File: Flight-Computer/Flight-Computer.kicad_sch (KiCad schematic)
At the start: 40 parts, among them J1 Jumper_NO, J2 Jumper_NO, P1 647676-2, P2 1546551-2, P3 3220-20-0200-00, U1 STM32H750VBTx, U2 LMS8117AMP-3.3_NOPB, Y1 ECS-240-18-33-JGN-TR

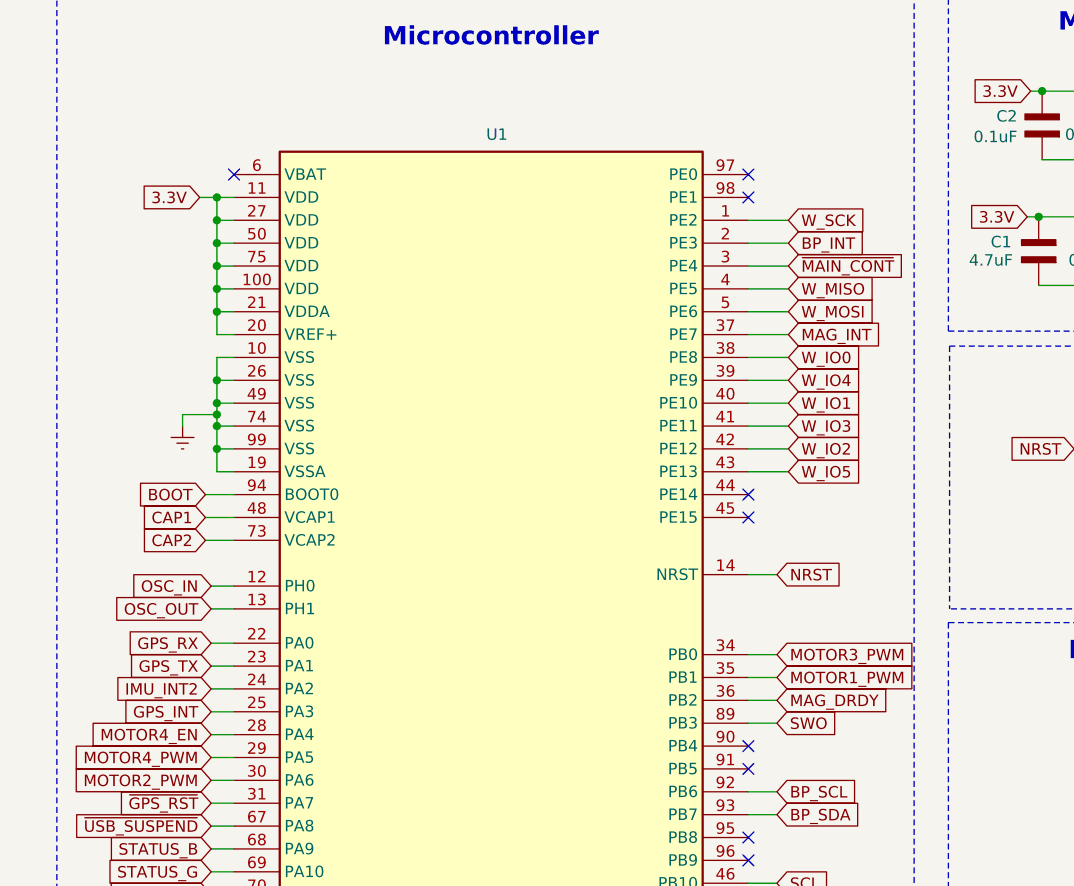
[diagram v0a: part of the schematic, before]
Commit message: SPI Flash Daisy chain
need to review and likely rewire the daisy chain
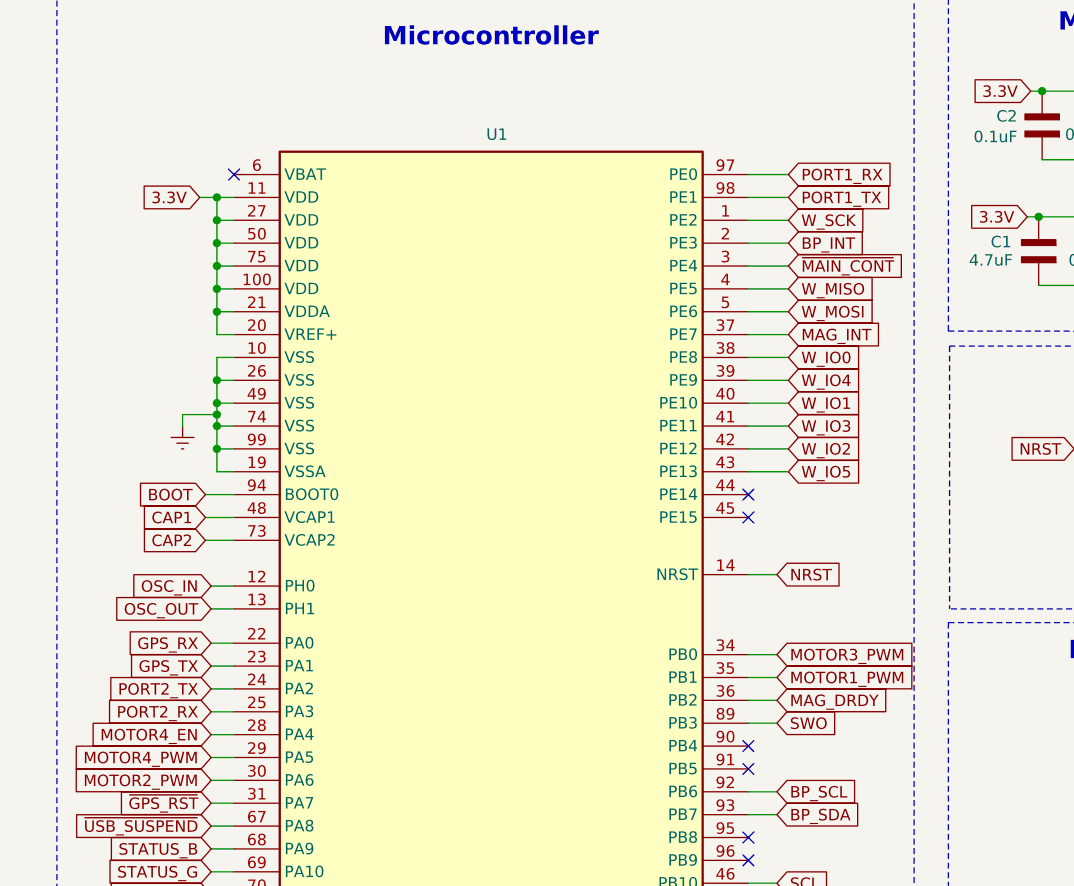
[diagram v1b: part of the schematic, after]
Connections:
- net PORT1_RX: now reaches U1.97 (PE0)
- net PORT1_TX: now reaches U1.98 (PE1)
- net GPS_INT renamed PORT2_RX
- net IMU_INT2 renamed PORT2_TX
- no-connect marks 22 -> 20
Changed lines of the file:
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@@
 	)
 	(no_connect
-		(at 93.345 43.815)
-	)
-	(no_connect
 		(at 93.345 117.475)
 	)
@@
 	)
 	(no_connect
-		(at 93.345 41.275)
-	)
-	(no_connect
 		(at 93.345 107.315)
 	)
@@
 	(wire
 		(pts
+			(xy 97.79 41.275) (xy 93.345 41.275)
+		)
+		(stroke
+			(width 0)
+			(type default)
+		)
+	)
+	(wire
+		(pts
 			(xy 206.375 106.68) (xy 208.28 106.68)
 		)
@@
 	(wire
 		(pts
+			(xy 97.79 43.815) (xy 93.345 43.815)
+		)
+		(stroke
+			(width 0)
+			(type default)
+		)
+	)
+	(wire
+		(pts
 			(xy 93.345 56.515) (xy 97.79 56.515)
 		)
@@
 		)
 	)
+	(global_label "PORT1_TX"
+		(shape input)
+		(at 97.79 43.815 0)
+		(fields_autoplaced yes)
+		(effects
+			(font
+				(size 1.27 1.27)
+			)
+			(justify left)
+		)
+		(property "Intersheetrefs" "${INTERSHEET_REFS}"
+			(at 109.3133 43.815 0)
+			(effects
+				(font
+					(size 1.27 1.27)
+				)
+				(justify left)
+				(hide yes)
+			)
+		)
+	)
 	(global_label "MOTOR1_PWM"
 		(shape input)
@@
 		)
 	)
+	(global_label "PORT2_RX"
+		(shape input)
+		(at 33.655 100.965 180)
+		(fields_autoplaced yes)
+		(effects
+			(font
+				(size 1.27 1.27)
+			)
+			(justify right)
+		)
+		(property "Intersheetrefs" "${INTERSHEET_REFS}"
+			(at 21.8293 100.965 0)
+			(effects
+				(font
+					(size 1.27 1.27)
+				)
+				(justify right)
+				(hide yes)
+			)
+		)
+	)
 	(global_label "BOOT"
 		(shape input)
@@
 		)
 	)
-	(global_label "GPS_INT"
-		(shape input)
-		(at 33.655 100.965 180)
-		(fields_autoplaced yes)
-		(effects
-			(font
-				(size 1.27 1.27)
-			)
-			(justify right)
-		)
-		(property "Intersheetrefs" "${INTERSHEET_REFS}"
-			(at 23.7108 100.8856 0)
-			(effects
-				(font
-					(size 1.27 1.27)
-				)
-				(justify right)
-				(hide yes)
-			)
-		)
-	)
 	(global_label "W_IO2"
 		(shape input)
@@
 		)
 	)
-	(global_label "IMU_INT2"
-		(shape input)
-		(at 33.655 98.425 180)
-		(fields_autoplaced yes)
-		(effects
-			(font
-				(size 1.27 1.27)
-			)
-			(justify right)
-		)
-		(property "Intersheetrefs" "${INTERSHEET_REFS}"
-			(at 22.8641 98.3456 0)
-			(effects
-				(font
-					(size 1.27 1.27)
-				)
-				(justify right)
-				(hide yes)
-			)
-		)
-	)
 	(global_label "CAP2"
 		(shape input)
@@
 		)
 	)
+	(global_label "PORT2_TX"
+		(shape input)
+		(at 33.655 98.425 180)
+		(fields_autoplaced yes)
+		(effects
+			(font
+				(size 1.27 1.27)
+			)
+			(justify right)
+		)
+		(property "Intersheetrefs" "${INTERSHEET_REFS}"
+			(at 22.1317 98.425 0)
+			(effects
+				(font
+					(size 1.27 1.27)
+				)
+				(justify right)
+				(hide yes)
+			)
+		)
+	)
 	(global_label "MOTOR1_EN"
 		(shape input)
@@
 			(effects
 				(font
+					(size 1.27 1.27)
+				)
+				(justify left)
+				(hide yes)
+			)
+		)
+	)
+	(global_label "PORT1_RX"
+		(shape input)
+		(at 97.79 41.275 0)
+		(fields_autoplaced yes)
+		(effects
+			(font
+				(size 1.27 1.27)
+			)
+			(justify left)
+		)
+		(property "Intersheetrefs" "${INTERSHEET_REFS}"
+			(at 109.6157 41.275 0)
+			(effects
+				(font
